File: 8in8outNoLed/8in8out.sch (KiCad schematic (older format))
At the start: 90 parts, among them IC1 ATTINY2313-P, J1 RJ45, J2 RJ45, J3 CONN_6, K110 G5T-1-12VDC, K120 G5T-1-12VDC, K130 G5T-1-12VDC, K140 G5T-1-12VDC, K150 G5T-1-12VDC, K160 G5T-1-12VDC, K170 G5T-1-12VDC, K180 G5T-1-12VDC, P1 CONN_5, P100 CONN_2, P101 CONN_2, P102 CONN_2, P103 CONN_2, P105 CONN_2, P106 CONN_2, P107 CONN_8, P109 CONN_2, P110 CONN_2, P120 CONN_2, P130 CONN_2, P140 CONN_2, P150 CONN_2, P160 CONN_2, P170 CONN_2, P180 CONN_2, P2 CONN_5, Q110 NPN, Q120 NPN, Q130 NPN, Q140 NPN, Q150 NPN, Q160 NPN, Q170 NPN, Q180 NPN, U1 74HC595, U10 OPTO-TRANSISTOR, U2 74LS165, U20 OPTO-TRANSISTOR, U30 OPTO-TRANSISTOR, U40 OPTO-TRANSISTOR, U50 OPTO-TRANSISTOR, U60 OPTO-TRANSISTOR, U70 OPTO-TRANSISTOR, U80 OPTO-TRANSISTOR

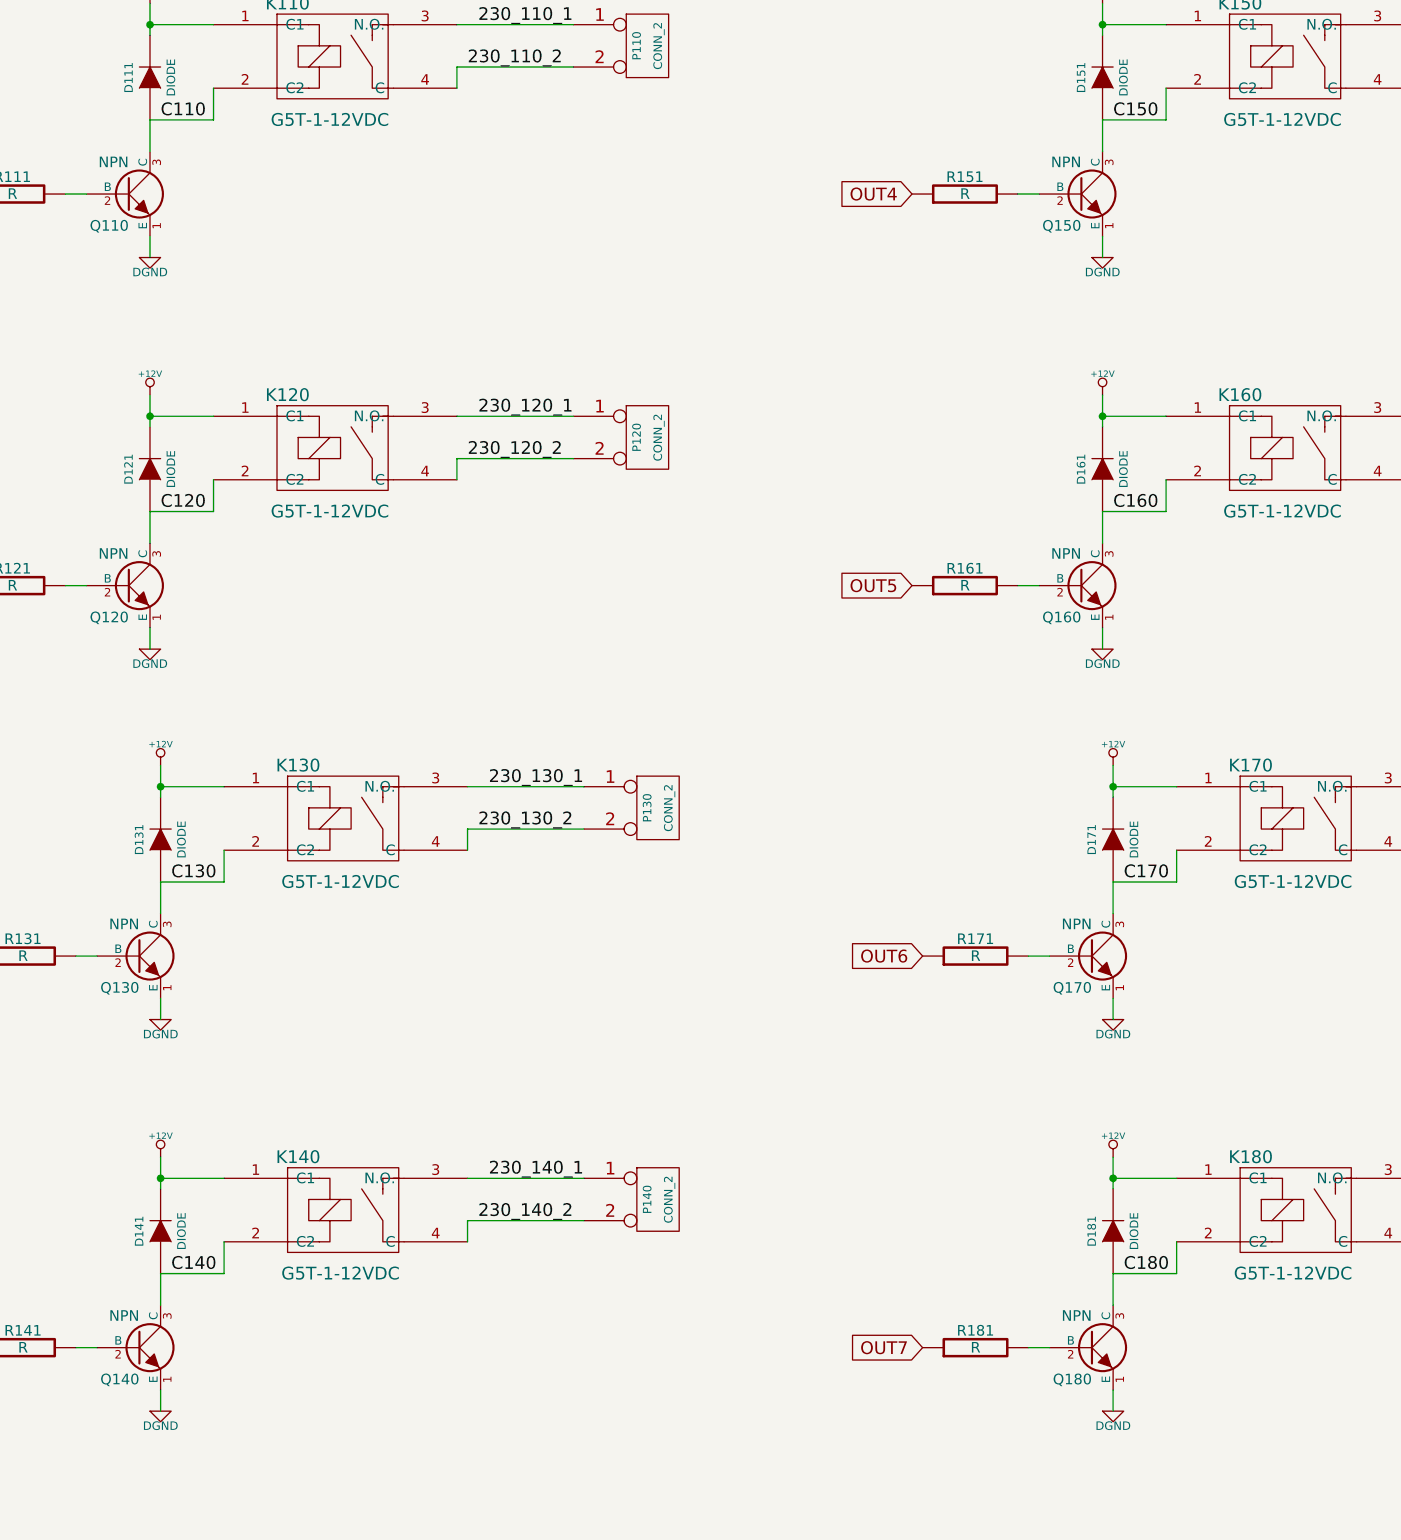
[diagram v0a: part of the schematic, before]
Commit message: ajout deux points par relais pour bypasser le NPN et commander le relais en direct (mode secours update .brd
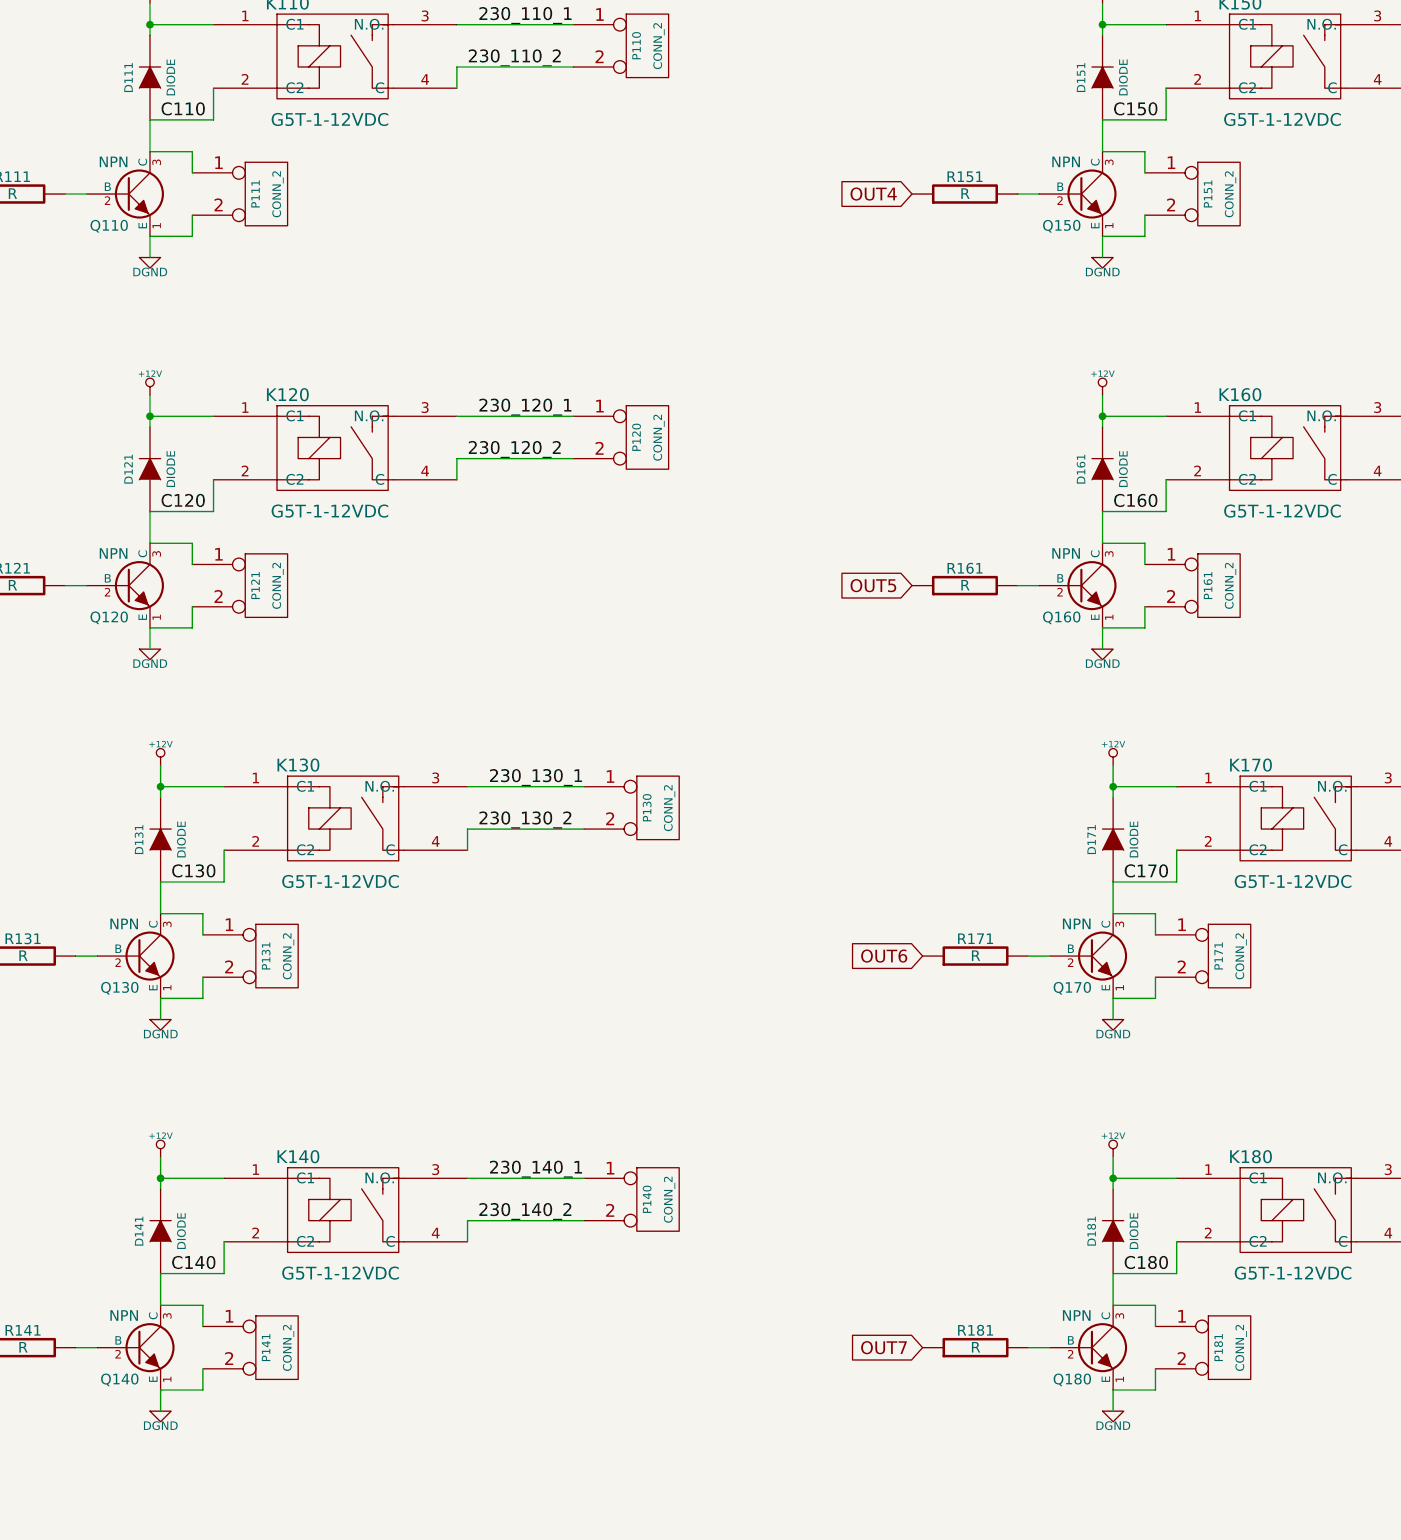
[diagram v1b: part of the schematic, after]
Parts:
- added P111, P121, P131, P141, P151, P161, P171, P181: CONN_2, symbol CONN_2
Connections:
- net C110: now also P111.1 (P1)
- net C120: now also P121.1 (P1)
- net C130: now also P131.1 (P1)
- net C140: now also P141.1 (P1)
- net C150: now also P151.1 (P1)
- net C160: now also P161.1 (P1)
- net C170: now also P171.1 (P1)
- net C180: now also P181.1 (P1)
- net DGND: now also P111.2 (PM), P121.2 (PM), P131.2 (PM), P141.2 (PM), P151.2 (PM), P161.2 (PM), P171.2 (PM), P181.2 (PM)
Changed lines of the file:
@@
-EESchema Schematic File Version 2  date mar. 12 févr. 2013 22:02:14 CET
+EESchema Schematic File Version 2  date mer. 13 févr. 2013 18:12:19 CET
 LIBS:g5la-1-12vdc
 LIBS:power
@@
 Sheet 1 1
 Title "8in 8relays I2C board"
-Date "12 feb 2013"
+Date "13 feb 2013"
 Rev "V0.0"
 Comp "XPLDUINO project"
@@
 	1    0    0    -1
 $EndComp
+$Comp
+L CONN_2 P111
+U 1 1 511BCD15
+P 15750 5300
+F 0 "P111" V 15700 5300 40  0000 C CNN
+F 1 "CONN_2" V 15800 5300 40  0000 C CNN
+	1    15750 5300
+	1    0    0    -1
+$EndComp
+$Comp
+L CONN_2 P121
+U 1 1 511BCD1B
+P 15750 7150
+F 0 "P121" V 15700 7150 40  0000 C CNN
+F 1 "CONN_2" V 15800 7150 40  0000 C CNN
+	1    15750 7150
+	1    0    0    -1
+$EndComp
+$Comp
+L CONN_2 P131
+U 1 1 511BCD2B
+P 15800 8900
+F 0 "P131" V 15750 8900 40  0000 C CNN
+F 1 "CONN_2" V 15850 8900 40  0000 C CNN
+	1    15800 8900
+	1    0    0    -1
+$EndComp
+$Comp
+L CONN_2 P141
+U 1 1 511BCD31
+P 15800 10750
+F 0 "P141" V 15750 10750 40  0000 C CNN
+F 1 "CONN_2" V 15850 10750 40  0000 C CNN
+	1    15800 10750
+	1    0    0    -1
+$EndComp
+Wire Wire Line
+	15250 10550 15450 10550
+Wire Wire Line
+	15450 10550 15450 10650
+Wire Wire Line
+	15250 10950 15450 10950
+Wire Wire Line
+	15450 10950 15450 10850
+Wire Wire Line
+	15450 9000 15450 9100
+Wire Wire Line
+	15250 8700 15450 8700
+Wire Wire Line
+	15450 8700 15450 8800
+Wire Wire Line
+	15450 9100 15250 9100
+Wire Wire Line
+	15200 6950 15400 6950
+Wire Wire Line
+	15400 6950 15400 7050
+Wire Wire Line
+	15200 7350 15400 7350
+Wire Wire Line
+	15400 7350 15400 7250
+Wire Wire Line
+	15200 5100 15400 5100
+Wire Wire Line
+	15400 5100 15400 5200
+Wire Wire Line
+	15200 5500 15400 5500
+Wire Wire Line
+	15400 5500 15400 5400
+$Comp
+L CONN_2 P151
+U 1 1 511BDA19
+P 20250 5300
+F 0 "P151" V 20200 5300 40  0000 C CNN
+F 1 "CONN_2" V 20300 5300 40  0000 C CNN
+	1    20250 5300
+	1    0    0    -1
+$EndComp
+$Comp
+L CONN_2 P161
+U 1 1 511BDA1F
+P 20250 7150
+F 0 "P161" V 20200 7150 40  0000 C CNN
+F 1 "CONN_2" V 20300 7150 40  0000 C CNN
+	1    20250 7150
+	1    0    0    -1
+$EndComp
+$Comp
+L CONN_2 P171
+U 1 1 511BDA25
+P 20300 8900
+F 0 "P171" V 20250 8900 40  0000 C CNN
+F 1 "CONN_2" V 20350 8900 40  0000 C CNN
+	1    20300 8900
+	1    0    0    -1
+$EndComp
+$Comp
+L CONN_2 P181
+U 1 1 511BDA2B
+P 20300 10750
+F 0 "P181" V 20250 10750 40  0000 C CNN
+F 1 "CONN_2" V 20350 10750 40  0000 C CNN
+	1    20300 10750
+	1    0    0    -1
+$EndComp
+Wire Wire Line
+	19750 10550 19950 10550
+Wire Wire Line
+	19950 10550 19950 10650
+Wire Wire Line
+	19750 10950 19950 10950
+Wire Wire Line
+	19950 10950 19950 10850
+Wire Wire Line
+	19750 9100 19950 9100
+Wire Wire Line
+	19950 9100 19950 9000
+Wire Wire Line
+	19750 8700 19950 8700
+Wire Wire Line
+	19950 8700 19950 8800
+Wire Wire Line
+	19700 6950 19900 6950
+Wire Wire Line
+	19900 6950 19900 7050
+Wire Wire Line
+	19700 7350 19900 7350
+Wire Wire Line
+	19900 7350 19900 7250
+Wire Wire Line
+	19700 5100 19900 5100
+Wire Wire Line
+	19900 5100 19900 5200
+Wire Wire Line
+	19700 5500 19900 5500
+Wire Wire Line
+	19900 5500 19900 5400
 $EndSCHEMATC

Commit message: Mis au propre du sch?ma
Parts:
- U2: value 74LS165 -> 74HC165
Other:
- note added: "EXTENSION CONNECTOR"
- note added: "INPUTS GROUP 1"
- note added: "INPUTS GROUP 2"
- note added: "INPUTS SHIFT REGISTER (MULTIPLEXER)"
- note added: "OUTPUTS SHIFT REGISTER (MULTIPLEXER)"
- note added: "RELAYS"
- note added: "SERIAL LINK"
- moved on the sheet: C1, C2, D1, D111, D121, D131, D141, D151, D161, D171, D181, D2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

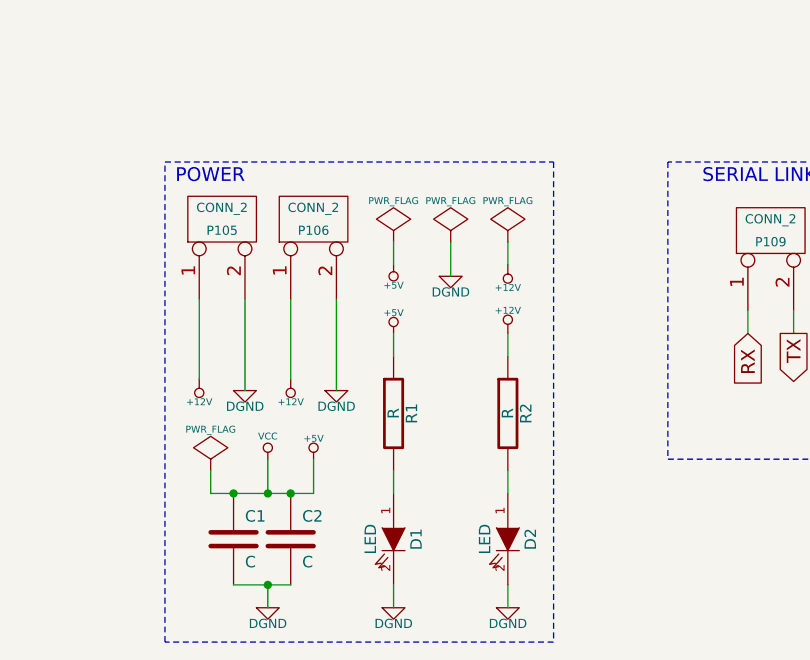
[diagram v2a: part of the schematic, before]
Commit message: ajout d'un connecteur 12v-Gnd-5v (P200)
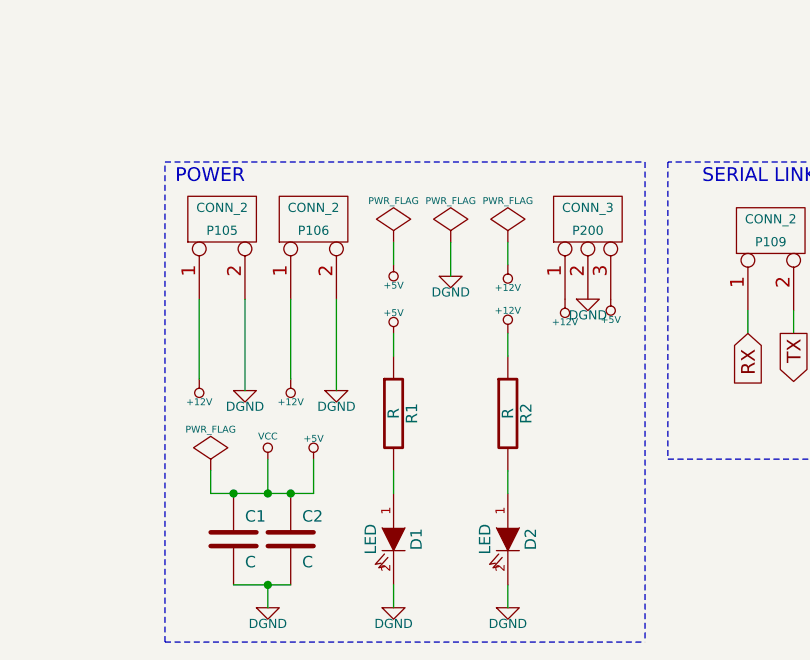
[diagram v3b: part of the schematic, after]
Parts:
- added P200: CONN_3, symbol CONN_3
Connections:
- net +12V: now also P200.1 (P1)
- net +5V: now also P200.3 (P3)
- net DGND: now also P200.2 (PM)
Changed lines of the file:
@@
-EESchema Schematic File Version 2  date mer. 13 févr. 2013 22:14:54 CET
+EESchema Schematic File Version 2  date jeu. 14 févr. 2013 20:12:08 CET
 LIBS:g5la-1-12vdc
 LIBS:power
@@
 Sheet 1 1
 Title "8in 8relays I2C board"
-Date "13 feb 2013"
+Date "14 feb 2013"
 Rev "V0.0"
 Comp "XPLDUINO project"
@@
 	10150 11150 10150 10300
 Wire Notes Line
-	14600 13700 12900 13700
+	12900 13700 15000 13700
 Wire Notes Line
 	12900 13700 12900 11600
 Wire Notes Line
-	12900 11600 14600 11600
-Wire Notes Line
-	14600 11600 14600 13700
+	12900 11600 15000 11600
 Wire Notes Line
 	1900 13600 5950 13600
@@
 Wire Wire Line
 	11000 12650 11000 12250
+$Comp
+L CONN_3 P200
+U 1 1 511D3A83
+P 14750 11850
+F 0 "P200" V 14700 11850 40  0000 C CNN
+F 1 "CONN_3" V 14800 11850 40  0000 C CNN
+	1    14750 11850
+	0    -1   -1   0
+$EndComp
+$Comp
+L +12V #PWR082
+U 1 1 511D3A9A
+P 14650 12200
+F 0 "#PWR082" H 14650 12150 20  0001 C CNN
+F 1 "+12V" H 14650 12300 30  0000 C CNN
+	1    14650 12200
+	-1   0    0    1
+$EndComp
+$Comp
+L DGND #PWR083
+U 1 1 511D3AA0
+P 14750 12200
+F 0 "#PWR083" H 14750 12200 40  0001 C CNN
+F 1 "DGND" H 14750 12130 40  0000 C CNN
+	1    14750 12200
+	1    0    0    -1
+$EndComp
+$Comp
+L +5V #PWR084
+U 1 1 511D3AA6
+P 14850 12200
+F 0 "#PWR084" H 14850 12290 20  0001 C CNN
+F 1 "+5V" H 14850 12290 30  0000 C CNN
+	1    14850 12200
+	-1   0    0    1
+$EndComp
+Wire Notes Line
+	15000 11600 15000 13700
 $EndSCHEMATC
